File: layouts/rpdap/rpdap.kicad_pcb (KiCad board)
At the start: 4 copper layers, 50 parts

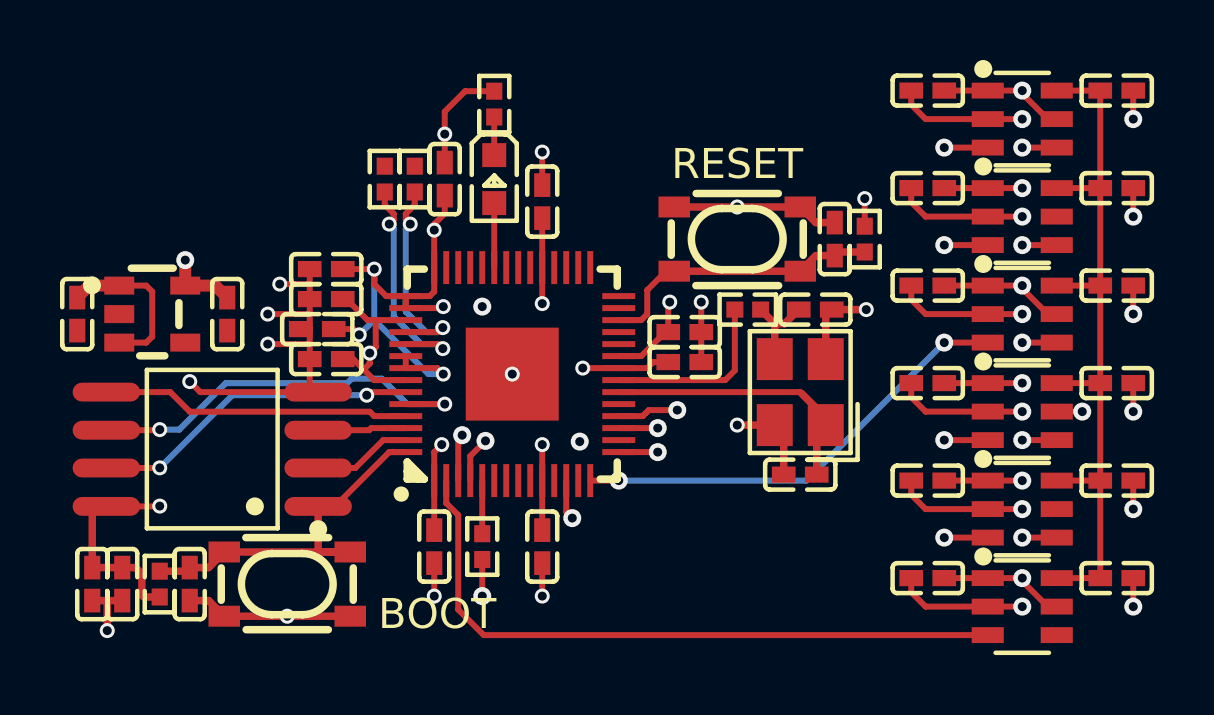
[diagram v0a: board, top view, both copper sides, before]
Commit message: update layouts and add jlink base compact layout
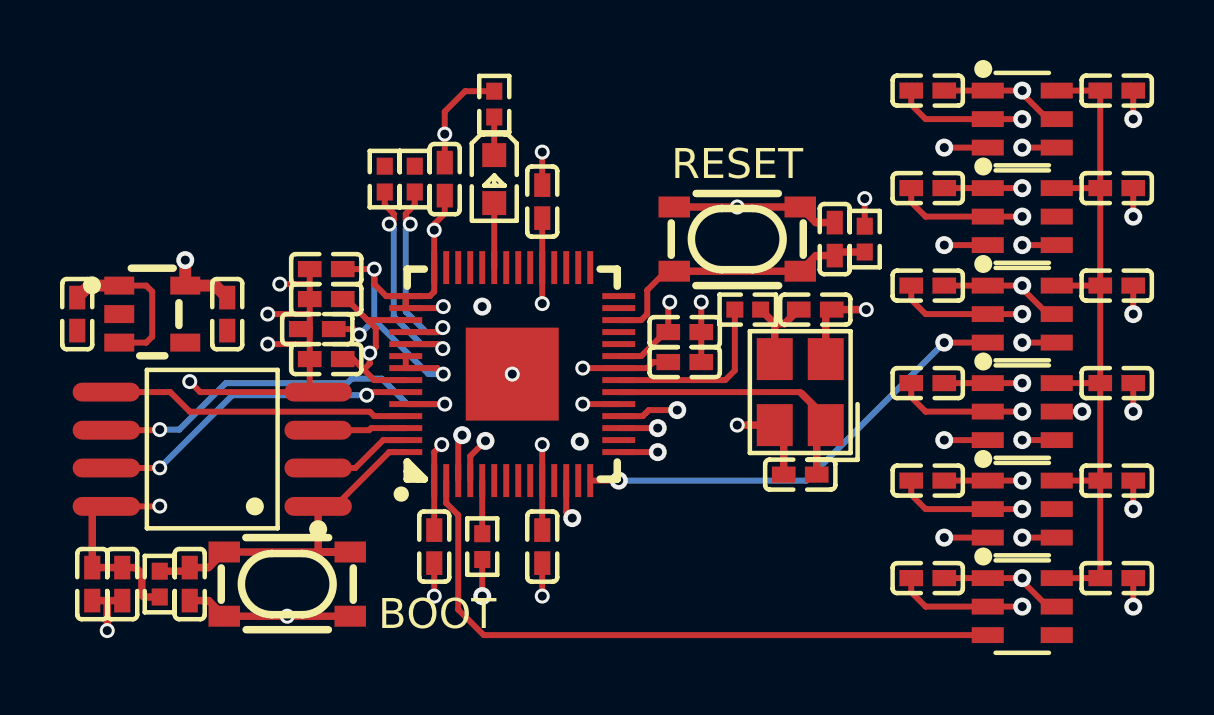
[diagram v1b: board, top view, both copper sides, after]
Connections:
- net GND_DETECT renamed TARGET_GND_DETECT
- net SWDIO renamed TARGET_SWDIO
- net SWO renamed TARGET_SWO
- net UART_RX renamed TARGET_UART_RX
- net UART_TX renamed TARGET_UART_TX
- net nRESET renamed TARGET_RESET
- U3 pad 4: -line-3 -> TARGET_SWCLK
- U4 pad 3: -line-4 -> -line-3
- U4 pad 5: (no net) -> GND
- U5 pad 3: -line-5 -> -line-4
- U6 pad 3: -line-6 -> -line-5
- U7 pad 3: -line-7 -> -line-6
- U7 pad 5: (no net) -> GND
- U8 pad 17: -line-4 -> -line-3
- U8 pad 18: -line-5 -> -line-4
- U8 pad 19: TESTEN -> GND
- U8 pad 2: -line-6 -> -line-5
- U8 pad 3: -line-7 -> -line-6
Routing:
- net -line-7: track 21.8 -> 0.00 mm, vias 2 -> 0
- net -line-3: track 1.15 -> 15.6 mm, vias 1 -> 2
- net -line-5: track 16.0 -> 22.5 mm, vias 2 -> 0
- net GND: track 72.5 -> 73.7 mm
- net TARGET_SWCLK: track 0.00 -> 1.15 mm, vias 0 -> 1
- net -line-6: track 22.5 -> 21.8 mm, vias 0 -> 2
- net QSPI_SCLK: vias 2 -> 3

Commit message: refactor jlink connector, make stick prety
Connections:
- net -line-0 renamed model-a-line-0
- net -line-1 renamed gpio[9]-line
- net -line-2 renamed model-a-line-1
- net -line-3 renamed gpio[14]-line
- net -line-4 renamed model-a-line-2
- net -line-5 renamed TX
- net -line-6 renamed RX
- net DVDD renamed _core_regulator_out_power-VCC
- net QSPI_SCLK renamed clock
- net QSPI_SS renamed chip_select
- net SWCLK renamed SWD_CLK
- net SWD renamed SWD_DIO
- net hv renamed power_b-VCC
- net mcu-line-0 renamed gpio[26]-line
- net mcu-line-1 renamed gpio[27]-line
- net mcu-line-2 renamed analog[2]-line
- net mcu-line-3 renamed gpio[29]-line
- net mcu-line-4 renamed SCLK
- net mcu-line-5 renamed MOSI
- net mcu-line-6 renamed MISO
- net mcu-line-7 renamed SDA
- net xin renamed XIN
- net xout renamed XOUT

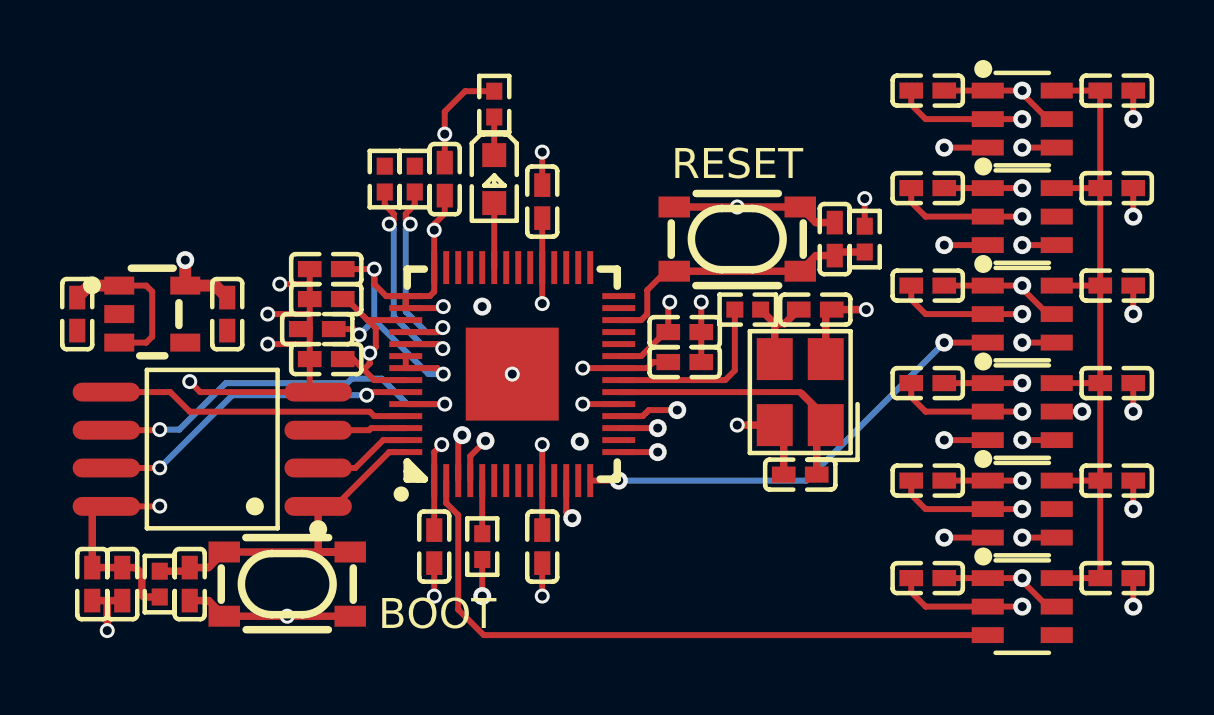
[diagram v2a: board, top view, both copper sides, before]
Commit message: refactor debug-connectors, fix issues in layout and connections
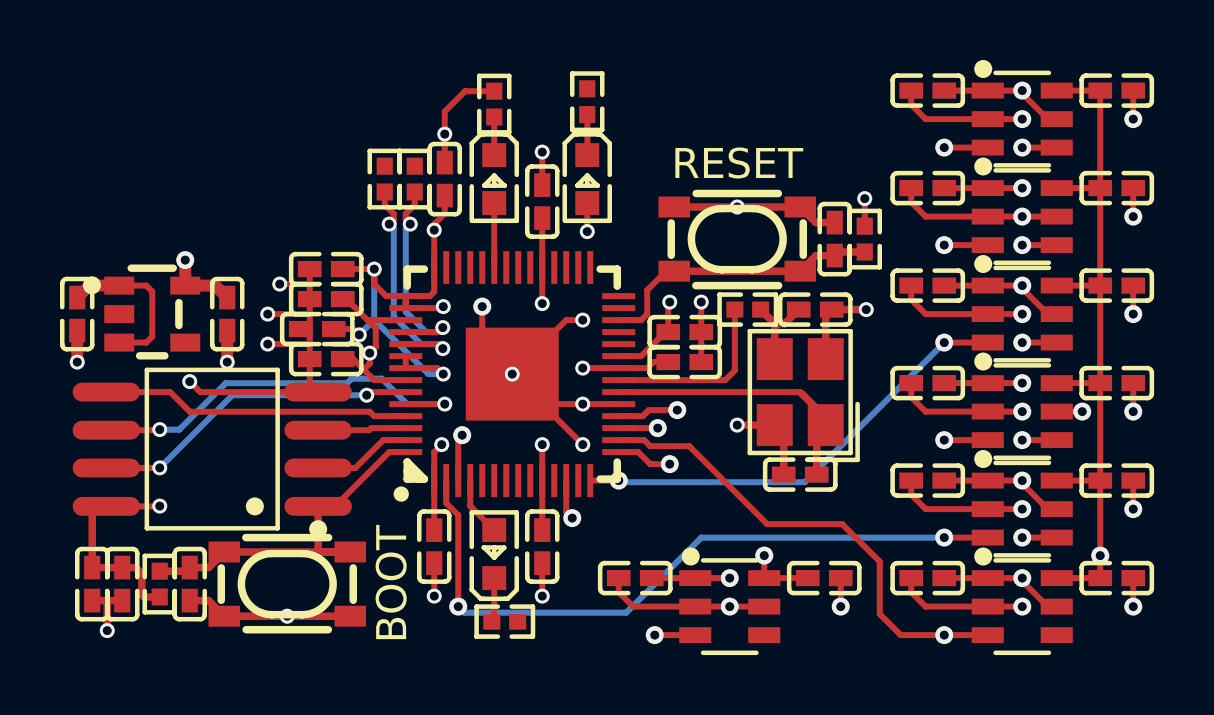
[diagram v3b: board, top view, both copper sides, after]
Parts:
- added C31: 100nF ±10% 16V X7R, Samsung_Electro_Mechanics_CL05B104KO5NNNC:C0402, F.Cu at (4.10, 6.80)
- added C32: 100nF ±10% 16V X7R, Samsung_Electro_Mechanics_CL05B104KO5NNNC:C0402, F.Cu at (10.4, 6.80)
- added LED2: , Hubei_KENTO_Elec_KT_0603R:LED0603-RD, F.Cu at (2.50, -6.50)
- added LED3: , Hubei_KENTO_Elec_Blue_light_0603:LED0603-RD, F.Cu at (-0.60, 6.00)
- added R8: 10kΩ ±1% 62.5mW, UNI_ROYAL_0402WGF1002TCE:R0402, F.Cu at (-0.25, 8.25)
- added U10: , Wuxi_I_core_Elec_AiP74LVC1T45GB236_TR:SOT-23-6_L2.9-W1.6-P0.95-LS2.8-BL, F.Cu at (7.25, 7.75)
- R1: value 100kΩ ±1% 62.5mW -> 1kΩ ±1% 62.5mW; footprint UNI_ROYAL_0402WGF1003TCE:R0402 -> UNI_ROYAL_0402WGF1001TCE:R0402
- moved R1 15.2 mm to (2.50, -9.08), turned to 90 degrees
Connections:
- net DI renamed data_0
- net DO renamed data_1
- net QSPI_SD2 renamed data_2
- net QSPI_SD3 renamed data_3
- net TARGET_RESET renamed nRESET
- net TARGET_SWCLK renamed TCK_SWCLK
- net TARGET_SWDIO renamed TMS_DIO
- net TARGET_SWO renamed TDO_SWO
- net TARGET_UART_RX renamed b-TX
- net TARGET_UART_TX renamed TDI
- net VBUS renamed power_shim-VCC
- net analog[2]-line renamed gpio[28]-line
- net gpio[9]-line renamed dir-line
- net power_b-VCC renamed VTREF
- C1 pad 2: GND -> vcp_indicator-power-GND-0
- C10 pad 2: GND -> vcp_indicator-power-GND-0
- C11 pad 2: GND -> vcp_indicator-power-GND-0
- C12 pad 2: GND -> vcp_indicator-power-GND-0
- C13 pad 2: GND -> vcp_indicator-power-GND-0
- C14 pad 2: GND -> vcp_indicator-power-GND-0
- C15 pad 2: GND -> vcp_indicator-power-GND-0
- C16 pad 2: GND -> vcp_indicator-power-GND-0
- C17 pad 2: GND -> vcp_indicator-power-GND-0
- C18 pad 2: GND -> vcp_indicator-power-GND-0
- C19 pad 2: GND -> vcp_indicator-power-GND-0
- C2 pad 2: GND -> vcp_indicator-power-GND-0
- C20 pad 2: GND -> vcp_indicator-power-GND-0
- C21 pad 2: GND -> vcp_indicator-power-GND-0
- C22 pad 2: GND -> vcp_indicator-power-GND-0
- C23 pad 2: GND -> vcp_indicator-power-GND-0
- C24 pad 2: GND -> vcp_indicator-power-GND-0
- C25 pad 2: GND -> vcp_indicator-power-GND-0
- C26 pad 2: GND -> vcp_indicator-power-GND-0
- C27 pad 2: GND -> vcp_indicator-power-GND-0
- C28 pad 2: GND -> vcp_indicator-power-GND-0
- C29 pad 2: GND -> vcp_indicator-power-GND-0
- C3 pad 2: GND -> vcp_indicator-power-GND-0
- C30 pad 2: GND -> vcp_indicator-power-GND-0
- C4 pad 2: GND -> vcp_indicator-power-GND-0
- C5 pad 2: GND -> vcp_indicator-power-GND-0
- C6 pad 2: GND -> vcp_indicator-power-GND-0
- C7 pad 2: GND -> vcp_indicator-power-GND-0
- C8 pad 2: GND -> vcp_indicator-power-GND-0
- C9 pad 2: GND -> vcp_indicator-power-GND-0
- R1 pad 1: TARGET_GND_DETECT -> footprint-cathode-0
- R1 pad 2: 3V3 -> vcp_indicator-power-GND-0
- R4 pad 1: GND -> vcp_indicator-power-GND-0
- SW1 pad 1: GND -> vcp_indicator-power-GND-0
- SW1 pad 2: GND -> vcp_indicator-power-GND-0
- SW2 pad 1: GND -> vcp_indicator-power-GND-0
- SW2 pad 2: GND -> vcp_indicator-power-GND-0
- U1 pad 2: GND -> vcp_indicator-power-GND-0
- U2 pad 2: GND -> vcp_indicator-power-GND-0
- U3 pad 2: GND -> vcp_indicator-power-GND-0
- U3 pad 5: 3V3 -> (no net)
- U4 pad 2: GND -> vcp_indicator-power-GND-0
- U4 pad 3: gpio[14]-line -> model-a-line-2
- U4 pad 5: GND -> vcp_indicator-power-GND-0
- U5 pad 2: GND -> vcp_indicator-power-GND-0
- U5 pad 3: model-a-line-2 -> model-a-line-3
- U5 pad 5: 3V3 -> (no net)
- U6 pad 2: GND -> vcp_indicator-power-GND-0
- U6 pad 3: TX -> model-a-line-4
- U6 pad 5: 3V3 -> (no net)
- U7 pad 2: GND -> vcp_indicator-power-GND-0
- U7 pad 3: RX -> a-TX
- U7 pad 5: GND -> (no net)
- U8 pad 16: GPIO13 -> model-a-line-4
- U8 pad 17: gpio[14]-line -> model-a-line-2
- U8 pad 18: model-a-line-2 -> model-a-line-3
- U8 pad 19: GND -> vcp_indicator-power-GND-0
- U8 pad 2: TX -> a-TX
- U8 pad 3: RX -> a-RX
- U8 pad 4: SDA -> anode
- U8 pad 5: TARGET_GND_DETECT -> SCL
- U8 pad 57: GND -> vcp_indicator-power-GND-0
- U9 pad 4: GND -> vcp_indicator-power-GND-0
- X1 pad 2: GND -> vcp_indicator-power-GND-0
- X1 pad 4: GND -> vcp_indicator-power-GND-0
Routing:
- net vcp_indicator-power-GND-1: track 0.00 -> 95.3 mm, vias 0 -> 32
- net GND: track 73.7 -> 0.00 mm, vias 29 -> 0
- net a-TX: track 0.00 -> 23.2 mm, vias 0 -> 2
- net TX: track 22.5 -> 0.00 mm
- net RX: track 21.8 -> 0.00 mm, vias 2 -> 0
- net model-a-line-4: track 0.00 -> 16.0 mm, vias 0 -> 1
- net model-a-line-3: track 0.00 -> 16.0 mm, vias 0 -> 2
- net gpio[14]-line: track 15.6 -> 0.00 mm, vias 2 -> 0
- net a-RX: track 0.00 -> 13.4 mm, vias 0 -> 2
- net VTREF: track 25.0 -> 38.4 mm, vias 0 -> 2
- net 3V3: track 60.8 -> 64.7 mm, vias 19 -> 20
- net anode: track 0.00 -> 1.98 mm
- net TARGET_GND_DETECT: track 1.77 -> 0.00 mm
- net SDA: track 1.53 -> 0.00 mm, vias 1 -> 0
- net footprint-cathode-1: track 0.00 -> 1.48 mm
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
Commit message: rebuild, small fixes, update README
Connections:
- net vcp_indicator-power-GND-0 renamed GND
- U3 pad 5: (no net) -> 3V3
- U5 pad 5: (no net) -> 3V3
- U6 pad 5: (no net) -> 3V3
- U7 pad 5: (no net) -> 3V3
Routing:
- net vcp_indicator-power-GND-1: track 95.3 -> 0.00 mm, vias 32 -> 0
- net (no net): track 0.00 -> 95.3 mm, vias 3 -> 35

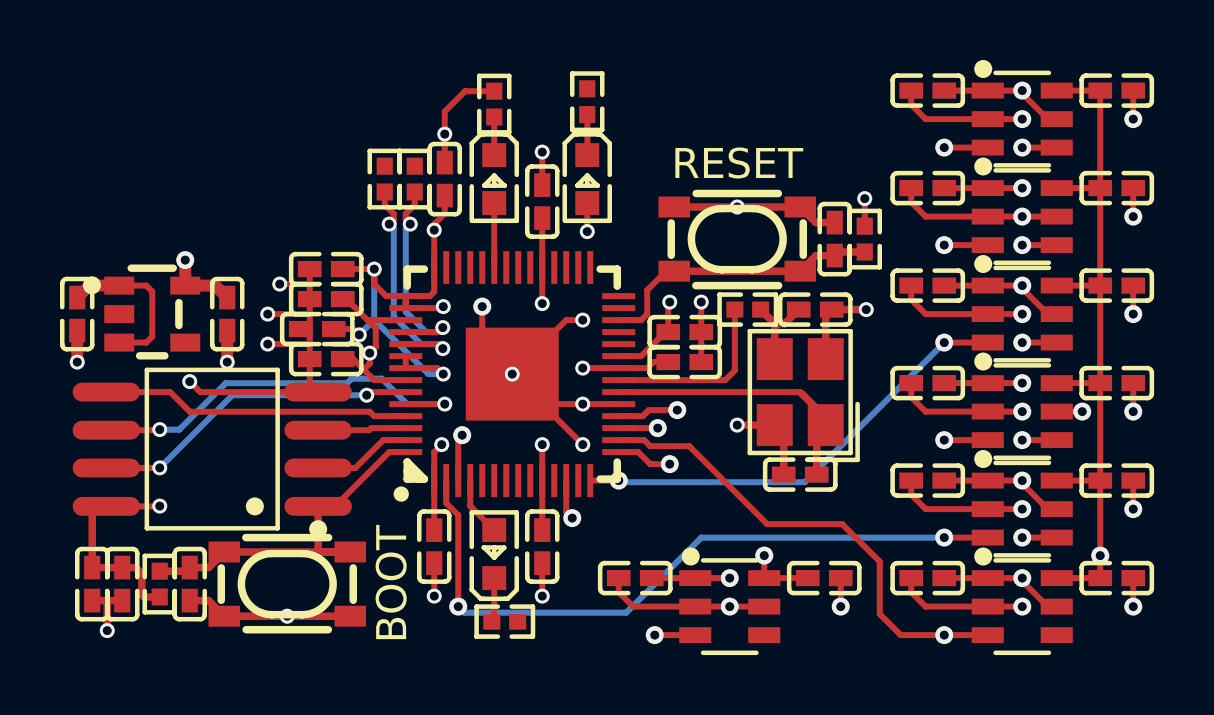
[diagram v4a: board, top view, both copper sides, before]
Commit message: fix: Update deps, swapped pinout (#2)
* rebuild with upstream rp2040 fixes. move header .25mm to the right. center dap-LED

* fix workflow triggers

* fix swapped jlink connector pinout + update deps

* pin atopile workflow version to v1.x.x
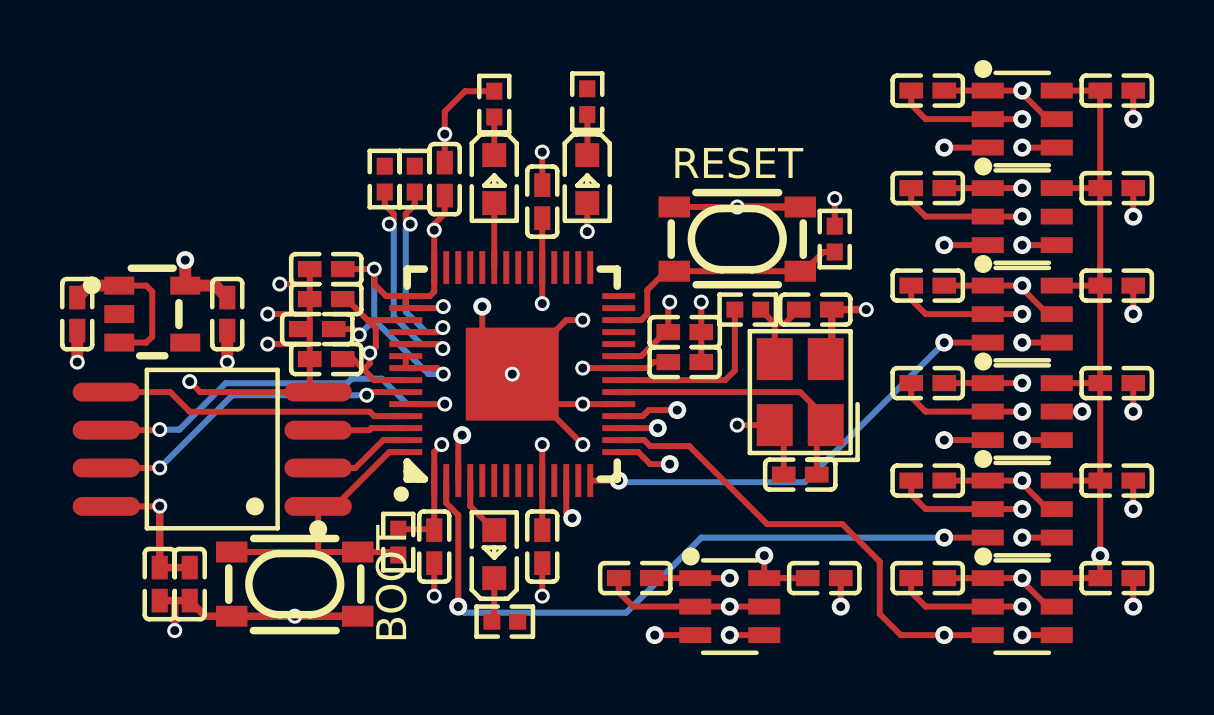
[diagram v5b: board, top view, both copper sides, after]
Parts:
- removed C15, C30: 1µF ±10% 25V X5R, Samsung_Electro_Mechanics_CL05A105KA5NQNC:C0402
- C16, C21, C28: value 2.2µF ±20% 6.3V X5R -> 2.2µF ±10% 16V X5R; footprint Samsung_Electro_Mechanics_CL05A225MQ5NSNC:C0402 -> Samsung_Electro_Mechanics_CL05A225KO5NQNC:C0402
- R6, R7: footprint YAGEO_RC0402FR_0727RL:R0402 -> UNI_ROYAL_0402WGF270JTCE:R0402
- X1: footprint Yangxing_Tech_X322512MSB4SI:CRYSTAL-SMD_4P-L3.2-W2.5-BL -> Abracon_LLC_ABM8_272_T3:CRYSTAL-SMD_4P-L3.2-W2.5-BL
- moved R2 8.07 mm to (-3.80, 5.60)
- moved C28 2.25 mm to (-11.7, 7.00)
- moved C29 2.25 mm to (-10.8, 7.00)
- moved R5 1.00 mm to (10.8, -4.50), turned to 90 degrees
- moved SW1 0.25 mm to (-7.25, 7.00), turned to 0 degrees
- turned SW2 to 180 degrees
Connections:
- net A renamed input-A
- net RP_USB_N renamed output-USB_D_N
- net RP_USB_P renamed output-USB_D_P
- net USB_N renamed input-USB_D_N
- net USB_P renamed input-USB_D_P
- net _core_regulator_out_power-VCC renamed VCC
- net a-RX renamed uart-RX
- net a-TX renamed uart-TX
- net dir-line renamed DIR
- net model-a-line-0 renamed gpio[12]-A
- net model-a-line-1 renamed gpio[11]-A
- net model-a-line-2 renamed gpio[14]-A
- net model-a-line-3 renamed gpio[15]-A
- net model-a-line-4 renamed gpio[13]-A
- net power_shim-VCC renamed Vbus_fused
- R2 pad 1: 3V3 -> chip_select
- R2 pad 2: chip_select -> 3V3
- R5 pad 1: 3V3 -> RUN
- R5 pad 2: RUN -> 3V3
- SW1 pad 1: GND -> chip_select
- SW1 pad 2: GND -> chip_select
- SW1 pad 3: chip_select -> GND
- SW1 pad 4: chip_select -> GND
- SW2 pad 1: GND -> RUN
- SW2 pad 2: GND -> RUN
- SW2 pad 3: RUN -> GND
- SW2 pad 4: RUN -> GND
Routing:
- net (no net): track 95.3 -> 0.00 mm, vias 35 -> 3
- net GND: track 0.00 -> 93.0 mm, vias 0 -> 32
- net chip_select: track 12.9 -> 10.8 mm
- net b-RX: track 0.00 -> 1.15 mm, vias 0 -> 1
- net TDI: track 0.00 -> 1.15 mm, vias 0 -> 1
- net RUN: track 9.61 -> 8.61 mm
- net 3V3: track 64.7 -> 63.9 mm
